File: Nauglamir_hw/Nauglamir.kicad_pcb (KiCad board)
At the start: 2 copper layers, 54 x 54 mm, 70 parts, among them Q1 2N7002

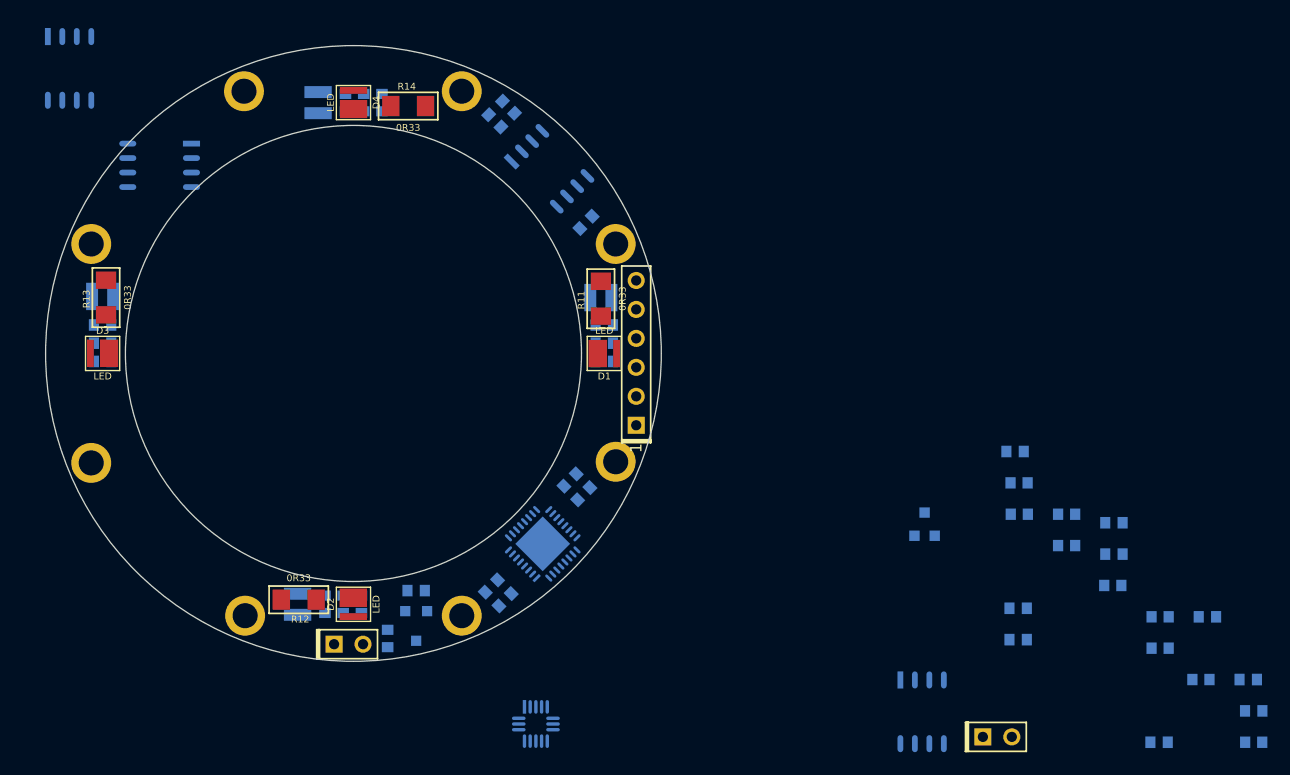
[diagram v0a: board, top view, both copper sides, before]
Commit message: PCB seems routed
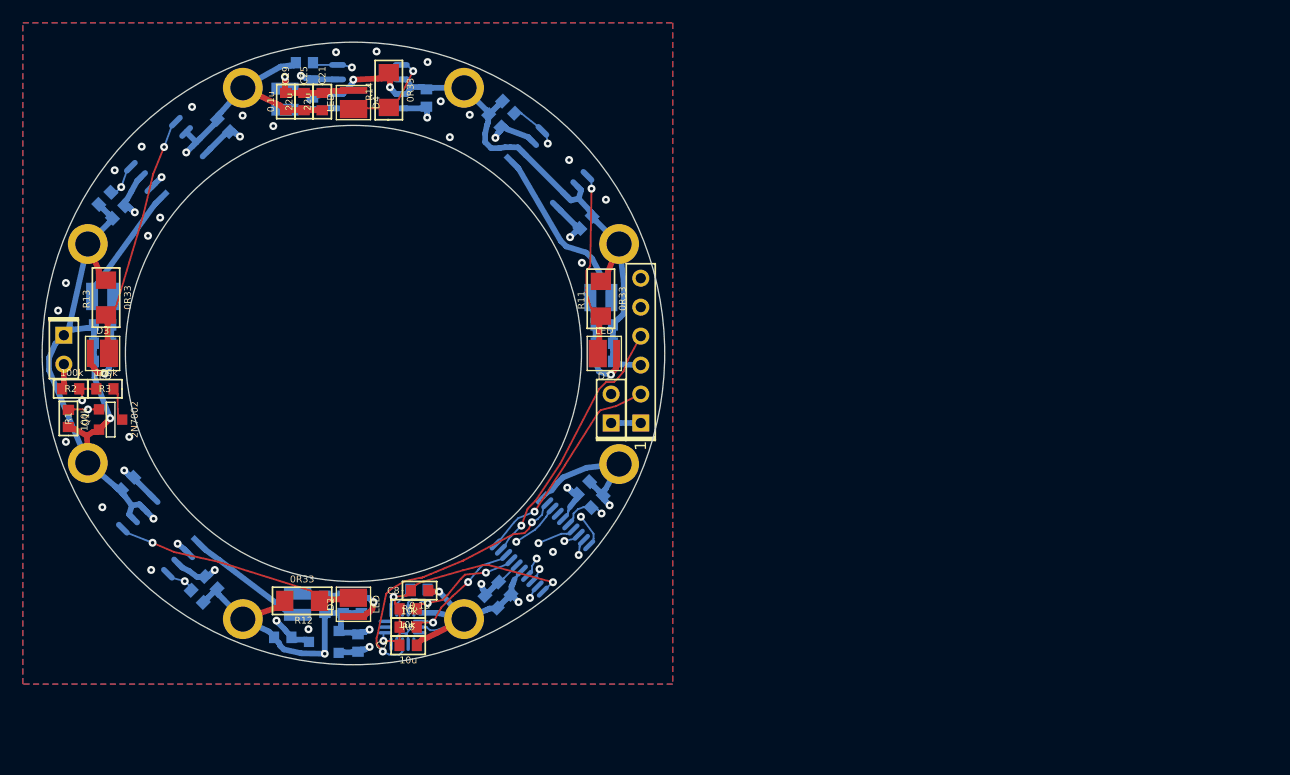
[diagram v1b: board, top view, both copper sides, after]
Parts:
- removed C3: 0.1u, Capacitors:CAP_0603_Silks
- C21, C25, C29, C7, C8, Q1, R1, R2, R3, R5, R6: moved to F.Cu
- DD1: value STM32F051KxUx -> STM32F030F6Px; footprint QFN_DFN:QFN-32_EP_5x5_Pitch0.5mm -> SO_DIL_TSSOP:TSSOP20
- moved C16 107.2 mm to (129.4, 87.6), turned to 225 degrees
- moved R3 105.4 mm to (128.2, 103.1), turned to 180 degrees
- moved R9 105.0 mm to (128.2, 86.4), turned to 225 degrees
- moved C11 100.8 mm to (130.2, 111.4), turned to 225 degrees
- moved R1 88.3 mm to (125.0, 105.7), turned to 90 degrees
- moved R2 88.0 mm to (125.2, 103.1), turned to 180 degrees
- moved C12 85.5 mm to (138.6, 80.0), turned to 135 degrees
- moved R10 84.4 mm to (145.7, 74.5), turned to 180 degrees
- moved C13 82.2 mm to (156.4, 77.6), turned to 90 degrees
- moved C15 79.2 mm to (137.5, 120.1), turned to 315 degrees
- moved R8 72.5 mm to (136.3, 121.3), turned to 315 degrees
- moved Q1 72.0 mm to (128.7, 105.8), turned to 90 degrees
- moved C17 69.4 mm to (146.4, 76.8), turned to 270 degrees
- moved DA3 68.5 mm to (133.1, 116.0), turned to 225 degrees
- moved C8 66.2 mm to (155.8, 120.8)
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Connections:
- DD1 pad 1: PwrMCU -> GND
- DD1 pad 10: (no net) -> /LED1_CTRL
- DD1 pad 11: /LED4_CTRL -> /ACC_PWR
- DD1 pad 12: /BAT_MEAS_EN -> /LED2_CTRL
- DD1 pad 13: /BAT_MEAS -> /LED3_CTRL
- DD1 pad 14: (no net) -> /LED4_CTRL
- DD1 pad 15: (no net) -> GND
- DD1 pad 16: (no net) -> PwrMCU
- DD1 pad 17: PwrMCU -> /I2C_SCL
- DD1 pad 18: (no net) -> /I2C_SDA
- DD1 pad 19: /UART_TX -> /SWDIO
- DD1 pad 2: (no net) -> /ACC_INT1
- DD1 pad 20: /UART_RX -> /SWCLK
- DD1 pad 3: (no net) -> /BAT_MEAS_EN
- DD1 pad 7: /LED1_CTRL -> /BAT_MEAS
- DD1 pad 8: /LED2_CTRL -> /UART_TX
- DD1 pad 9: /LED3_CTRL -> /UART_RX
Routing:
- net GND: track 0.00 -> 280.3 mm, vias 0 -> 36
- net +BATT: track 0.00 -> 130.9 mm, vias 0 -> 9
- net /LED3_CTRL: track 0.00 -> 72.6 mm, vias 0 -> 2
- net /LED4_CTRL: track 0.00 -> 58.5 mm, vias 0 -> 2
- net /BAT_MEAS: track 0.00 -> 53.6 mm, vias 0 -> 2
- net /BAT_MEAS_EN: track 0.00 -> 51.1 mm, vias 0 -> 2
- net PwrMCU: track 0.00 -> 45.3 mm, vias 0 -> 3
- net /LED1_CTRL: track 0.00 -> 40.6 mm, vias 0 -> 2
- net /LED2_CTRL: track 0.00 -> 35.2 mm, vias 0 -> 2
- net /UART_RX: track 0.00 -> 28.1 mm, vias 0 -> 1
- net /ACC_INT1: track 0.00 -> 24.7 mm, vias 0 -> 2
- net /UART_TX: track 0.00 -> 24.1 mm, vias 0 -> 1
- net /ACC_PWR: track 0.00 -> 24.1 mm, vias 0 -> 3
- net /SWDIO: track 0.00 -> 22.9 mm, vias 0 -> 1
- net Net-(D3-PadC): track 0.00 -> 21.7 mm, vias 0 -> 1
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- added copper zone on B.Cu, net GND
- added copper zone on F.Cu, net GND
- added copper zone on In1.Cu, net GND
- added copper zone on In2.Cu, net GND
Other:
- board size 54 x 54 mm -> 54.6 x 54.6 mm
- copper layers 2 -> 4
- net class Default: clearance 0.2 -> 0.15
- rule trace_clearance: 0.2 -> 0.15

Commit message: Routed
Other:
- rule pad_to_mask_clearance: 0 -> 0.06

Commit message: + Gerbers sent to factory
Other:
- board text added: "Nauglamir v1"
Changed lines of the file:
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@@
-(kicad_pcb (version 20190516) (host pcbnew "(5.1.0-815-gf49779465)")
+(kicad_pcb (version 20190516) (host pcbnew "(5.1.0-783-g669520924)")
   (general
     (thickness 1.6)
-    (drawings 19)
+    (drawings 21)
     (tracks 1124)
     (modules 69)
@@
     (38 "B.Mask" user)
     (39 "F.Mask" user hide)
-    (40 "Dwgs.User" user hide)
+    (40 "Dwgs.User" user)
     (44 "Edge.Cuts" user)
     (45 "Margin" user)
@@
     (visible_elements 7FFFFF7F)
     (pcbplotparams
-      (layerselection 0x010fc_ffffffff)
-      (usegerberextensions false)
+      (layerselection 0x010f0_ffffffff)
+      (usegerberextensions true)
       (usegerberattributes false)
       (usegerberadvancedattributes false)
@@
       (plotinvisibletext false)
       (padsonsilk false)
-      (subtractmaskfromsilk false)
+      (subtractmaskfromsilk true)
       (outputformat 1)
       (mirror false)
-      (drillshape 1)
+      (drillshape 0)
       (scaleselection 1)
-      (outputdirectory ""))
+      (outputdirectory "Gerber"))
   )
   (net 0 "")
@@
     )
   )
+  (dimension 54.6 (width 0.15) (layer "Dwgs.User")
+    (gr_text "54.600 mm" (at 150 131.5) (layer "Dwgs.User")
+      (effects (font (size 1 1) (thickness 0.15)))
+    )
+    (feature1 (pts (xy 177.3 100) (xy 177.3 130.786421)))
+    (feature2 (pts (xy 122.7 100) (xy 122.7 130.786421)))
+    (crossbar (pts (xy 122.7 130.2) (xy 177.3 130.2)))
+    (arrow1a (pts (xy 177.3 130.2) (xy 176.173496 130.786421)))
+    (arrow1b (pts (xy 177.3 130.2) (xy 176.173496 129.613579)))
+    (arrow2a (pts (xy 122.7 130.2) (xy 123.826504 130.786421)))
+    (arrow2b (pts (xy 122.7 130.2) (xy 123.826504 129.613579)))
+  )
+  (gr_text "Nauglamir\nv1" (at 128.6 102.3 270) (layer "B.SilkS")
+    (effects (font (size 1 1) (thickness 0.15)) (justify right mirror))
+  )
   (gr_circle (center 150 100) (end 175.2 100) (layer "Dwgs.User") (width 0.15))
   (gr_line (start 150 100) (end 177 111.2) (layer "Dwgs.User") (width 0.15))
@@
   (gr_circle (center 150 100) (end 177.3 100) (layer "Edge.Cuts") (width 0.1))
   (gr_circle (center 150 100) (end 170 100) (layer "Edge.Cuts") (width 0.1))
-  (segment (start 138.1296 118.7082) (end 138.6432 118.5246) (width 0.5) (layer "In2.Cu") (net 3))
-  (segment (start 138.1296 118.7082) (end 138.3258 118.1992) (width 0.5) (layer "In2.Cu") (net 3))
   (segment (start 168.8526 113.8161) (end 169.1223 113.5614) (width 0.16) (layer "B.Cu") (net 1))
   (segment (start 168.8526 113.8161) (end 168.8357 113.4456) (width 0.16) (layer "B.Cu") (net 1))
-  (segment (start 155.4526 122.7516) (end 155.7898 122.9061) (width 0.16) (layer "B.Cu") (net 2))
-  (segment (start 155.4526 122.7516) (end 155.7898 122.5971) (width 0.16) (layer "B.Cu") (net 2))
-  (segment (start 164.3466 119.5141) (end 164.0259 119.7005) (width 0.16) (layer "B.Cu") (net 2))
-  (segment (start 164.3466 119.5141) (end 164.2785 119.8787) (width 0.16) (layer "B.Cu") (net 2))
-  (segment (start 167.126 112.2706) (end 167.4472 112.1692) (width 0.16) (layer "B.Cu") (net 2))
-  (segment (start 167.126 112.2706) (end 167.2352 111.952) (width 0.16) (layer "B.Cu") (net 2))
   (segment (start 172.6 106.1) (end 172.1 106.6) (width 0.5) (layer "In2.Cu") (net 1))
   (segment (start 172.1 106.6) (end 171.85 106.85) (width 0.5) (layer "In2.Cu") (net 1))
@@
   (via (at 161.2174 120.2128) (size 0.7) (layers "F.Cu" "B.Cu") (net 1))
   (via (at 151.4181 125.7358) (size 0.7) (layers "F.Cu" "B.Cu") (net 1))
+  (segment (start 155.4526 122.7516) (end 155.7898 122.9061) (width 0.16) (layer "B.Cu") (net 2))
+  (segment (start 155.4526 122.7516) (end 155.7898 122.5971) (width 0.16) (layer "B.Cu") (net 2))
+  (segment (start 164.3466 119.5141) (end 164.0259 119.7005) (width 0.16) (layer "B.Cu") (net 2))
+  (segment (start 164.3466 119.5141) (end 164.2785 119.8787) (width 0.16) (layer "B.Cu") (net 2))
+  (segment (start 167.126 112.2706) (end 167.4472 112.1692) (width 0.16) (layer "B.Cu") (net 2))
+  (segment (start 167.126 112.2706) (end 167.2352 111.952) (width 0.16) (layer "B.Cu") (net 2))
   (segment (start 145.6662 78.6727) (end 145.4082 78.6727) (width 0.5) (layer "F.Cu") (net 2))
   (segment (start 145.4082 78.6727) (end 145.1582 78.6727) (width 0.5) (layer "F.Cu") (net 2))
@@
   (via (at 134.5796 116.688) (size 0.7) (layers "F.Cu" "B.Cu") (net 2))
   (via (at 151.418 124.2196) (size 0.7) (layers "F.Cu" "B.Cu") (net 2))
+  (segment (start 138.1296 118.7082) (end 138.6432 118.5246) (width 0.5) (layer "In2.Cu") (net 3))
+  (segment (start 138.1296 118.7082) (end 138.3258 118.1992) (width 0.5) (layer "In2.Cu") (net 3))
   (segment (start 124.45 103.1) (end 124.6 102.85) (width 0.5) (layer "F.Cu") (net 3))
   (segment (start 124.6 102.85) (end 124.6 102.6) (width 0.5) (layer "F.Cu") (net 3))
